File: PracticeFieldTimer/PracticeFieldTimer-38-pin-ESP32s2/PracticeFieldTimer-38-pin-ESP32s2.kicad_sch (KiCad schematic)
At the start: 17 parts, among them J1 RJ45, J2 4 x 20 I2C LCD, J3 DS3231 Module, J4 Panel, J5 RJ45, J6 Screw_Terminal_01x07, SW1 Reboot, SW2 Mode, SW3 Start/Cfg, U1 ESP32-DevKitC

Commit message: Clean up and assign most footprints. Need footprint for decoupling capacitor.
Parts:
- removed JP1: /CAN Enable, symbol Jumper:Jumper_2_Bridged
- added J1: /CAN Enable, Connector_PinHeader_2.54mm:PinHeader_1x02_P2.54mm_Vertical, symbol Connector:Conn_01x02_Pin
- D1, D2, D3: footprint (none) -> LED_THT:LED_D5.0mm
- J1, J5: footprint (none) -> Connector_RJ:RJ45_Amphenol_54602-x08_Horizontal
- J2: footprint (none) -> TerminalBlock:TerminalBlock_MaiXu_MX126-5.0-04P_1x04_P5.00mm
- J3: footprint (none) -> Connector_PinSocket_2.54mm:PinSocket_1x06_P2.54mm_Vertical
- J4: footprint (none) -> TerminalBlock:TerminalBlock_MaiXu_MX126-5.0-03P_1x03_P5.00mm
- J6: value Screw_Terminal_01x07 -> External Controls; footprint (none) -> TerminalBlock:TerminalBlock_MaiXu_MX126-5.0-07P_1x07_P5.00mm
- R3, R4: footprint (none) -> Resistor_THT:R_Axial_DIN0414_L11.9mm_D4.5mm_P5.08mm_Vertical
- SW1: footprint (none) -> Misc:SW_D6R40_F2_LFS
- SW2: footprint (none) -> Misc:2MS3T1B1M2QES
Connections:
- net GND: now also J1.2 (Pin_2)
- net at U1.10 (DAC_2/ADC2_CH9/GPIO26): now also J1.1 (Pin_1)

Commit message: Finish filling in footprints.
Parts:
- SW3: footprint (none) -> Misc:SW_D6R40_F2_LFS
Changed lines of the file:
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@@
 			)
 		)
-		(property "Footprint" ""
+		(property "Footprint" "Misc:SW_D6R40_F2_LFS"
 			(at 246.38 82.55 0)
 			(effects

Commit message: Resolved most errors. Still need to add mounting holes and define the board boundary. Also, the I2C header is way too close to the LCD and need to move. The required changes are unclear.
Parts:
- removed SW1: Reboot, Misc:SW_D6R40_F2_LFS, symbol Switch:SW_Push
- removed SW2: Mode, Misc:2MS3T1B1M2QES, symbol Switch:SW_SPDT
- removed SW3: Start/Cfg, Misc:SW_D6R40_F2_LFS, symbol Switch:SW_Push
- added S1: /RST, Misc:MJTP1119, symbol 2026-05-09_14-50-17:MJTP1119
- added S2: /CFG-START, Misc:MJTP1119, symbol 2026-05-09_14-50-17:MJTP1119
- added S3: 500ASSP1M2QE, Misc:SW_500ASSP1M2QE, symbol 2026-05-09_14-50-17:500ASSP1M2QE
- added U3: ~, Misc:LCD-I2C-20X4B-Breakout, symbol 2026-05-09_14-50-17:I2C_LCD_20x4
- J4: renamed from J3; footprint Connector_PinSocket_2.54mm:PinSocket_1x06_P2.54mm_Vertical -> Misc:DS3231_Module
- R3, R4: footprint Resistor_THT:R_Axial_DIN0414_L11.9mm_D4.5mm_P5.08mm_Vertical -> Resistor_THT:R_Axial_DIN0207_L6.3mm_D2.5mm_P15.24mm_Horizontal
- R5: footprint (none) -> Resistor_THT:R_Axial_DIN0207_L6.3mm_D2.5mm_P15.24mm_Horizontal
- renumbered J6 to J1, J4 to J3, J1 to J5, J5 to J6, J1 to J7
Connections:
- net GND: now also S1.1 (COM_1), S2.1 (COM_1), S3.2
- net /CFG-START: now also S2.2 (COM_2)
- net /Follow: now also S3.1
- net /Manual: now also S3.3
- net /RST: now also S1.2 (COM_2)
- no-connect marks 5 -> 28

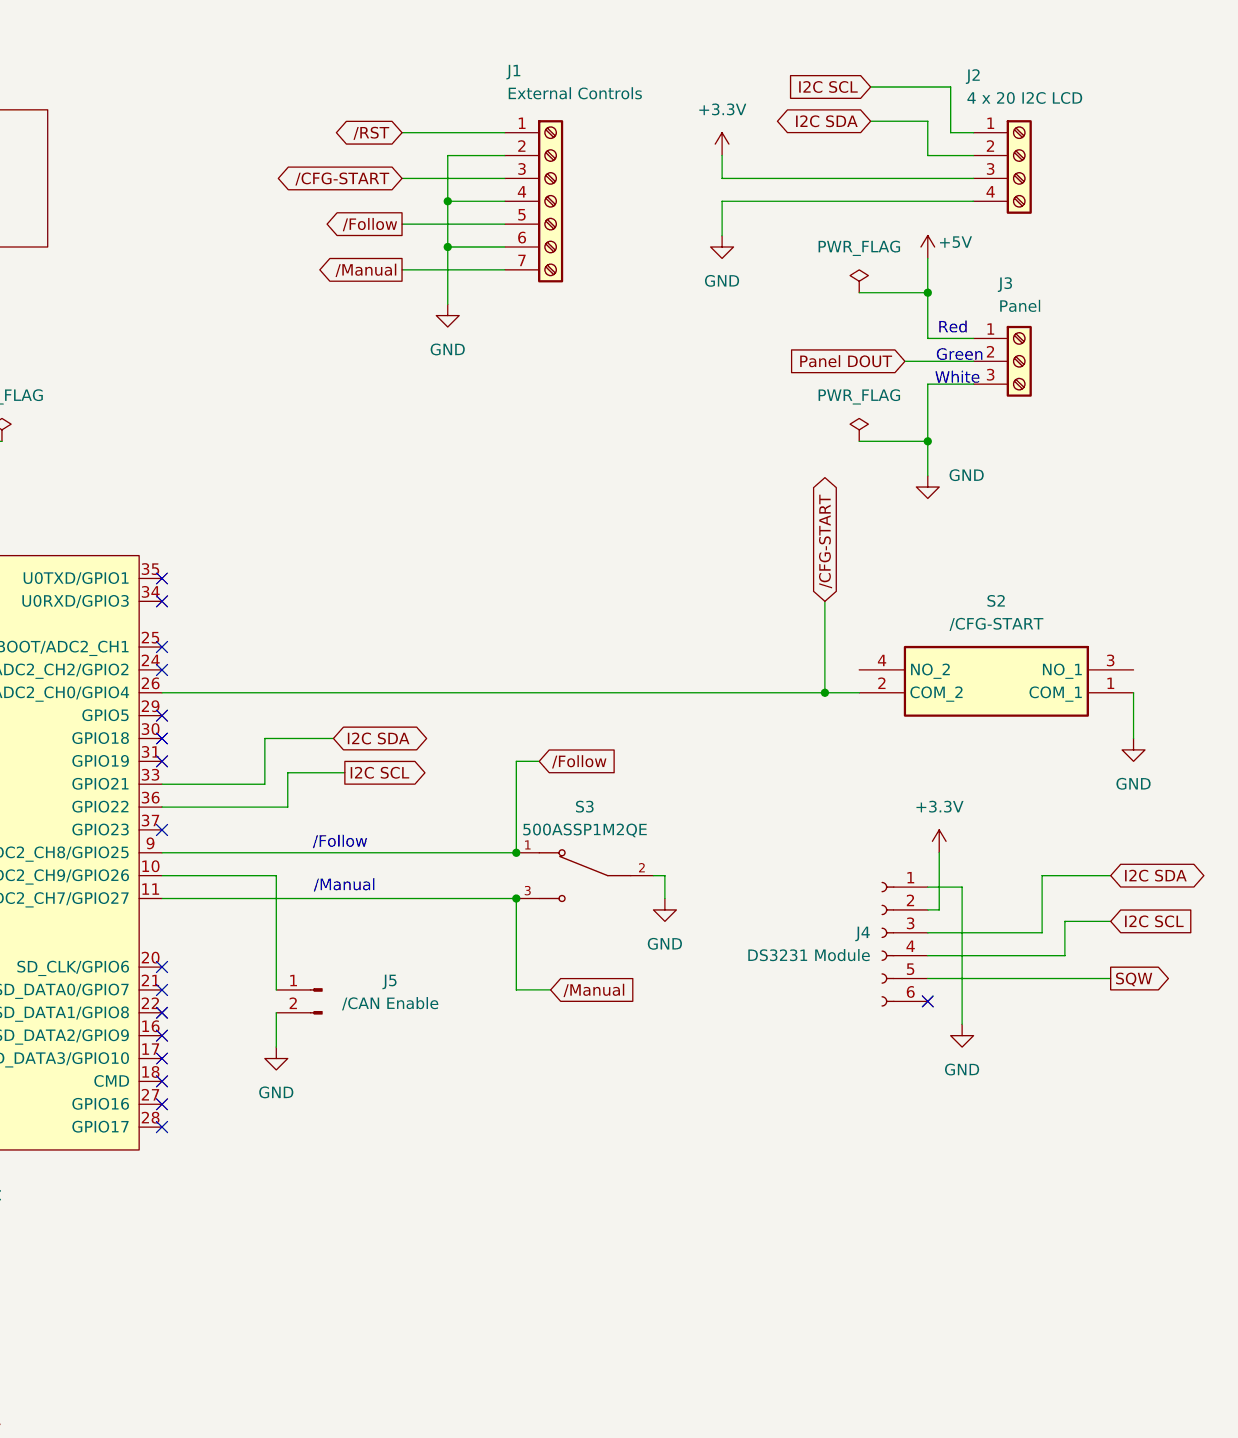
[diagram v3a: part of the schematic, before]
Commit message: Fix LCD header, which was wired backwards.
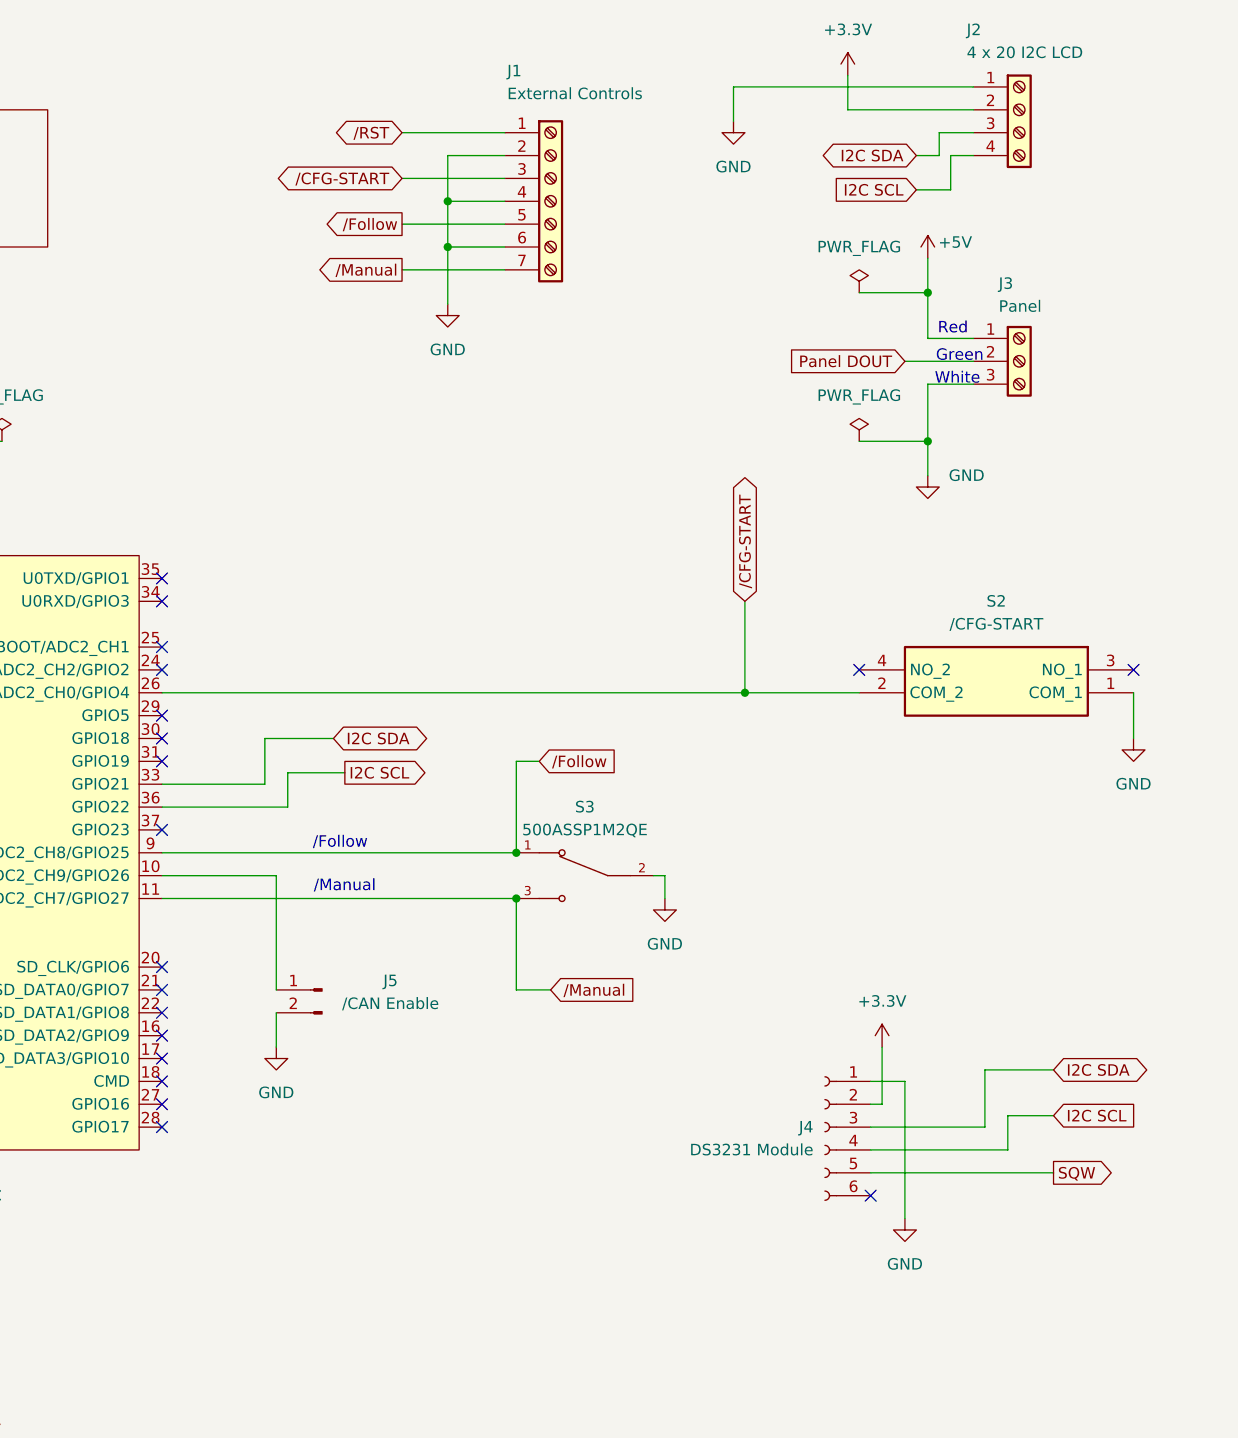
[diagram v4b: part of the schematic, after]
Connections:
- net +3.3V: now also J2.2 (Pin_2); no longer J2.3 (Pin_3)
- net GND: now also J2.1 (Pin_1); no longer J2.4 (Pin_4)
- net I2C SCL: now also J2.4 (Pin_4); no longer J2.1 (Pin_1)
- net I2C SDA: now also J2.3 (Pin_3); no longer J2.2 (Pin_2)
- no-connect marks 28 -> 30
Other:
- moved on the sheet: J2, J4

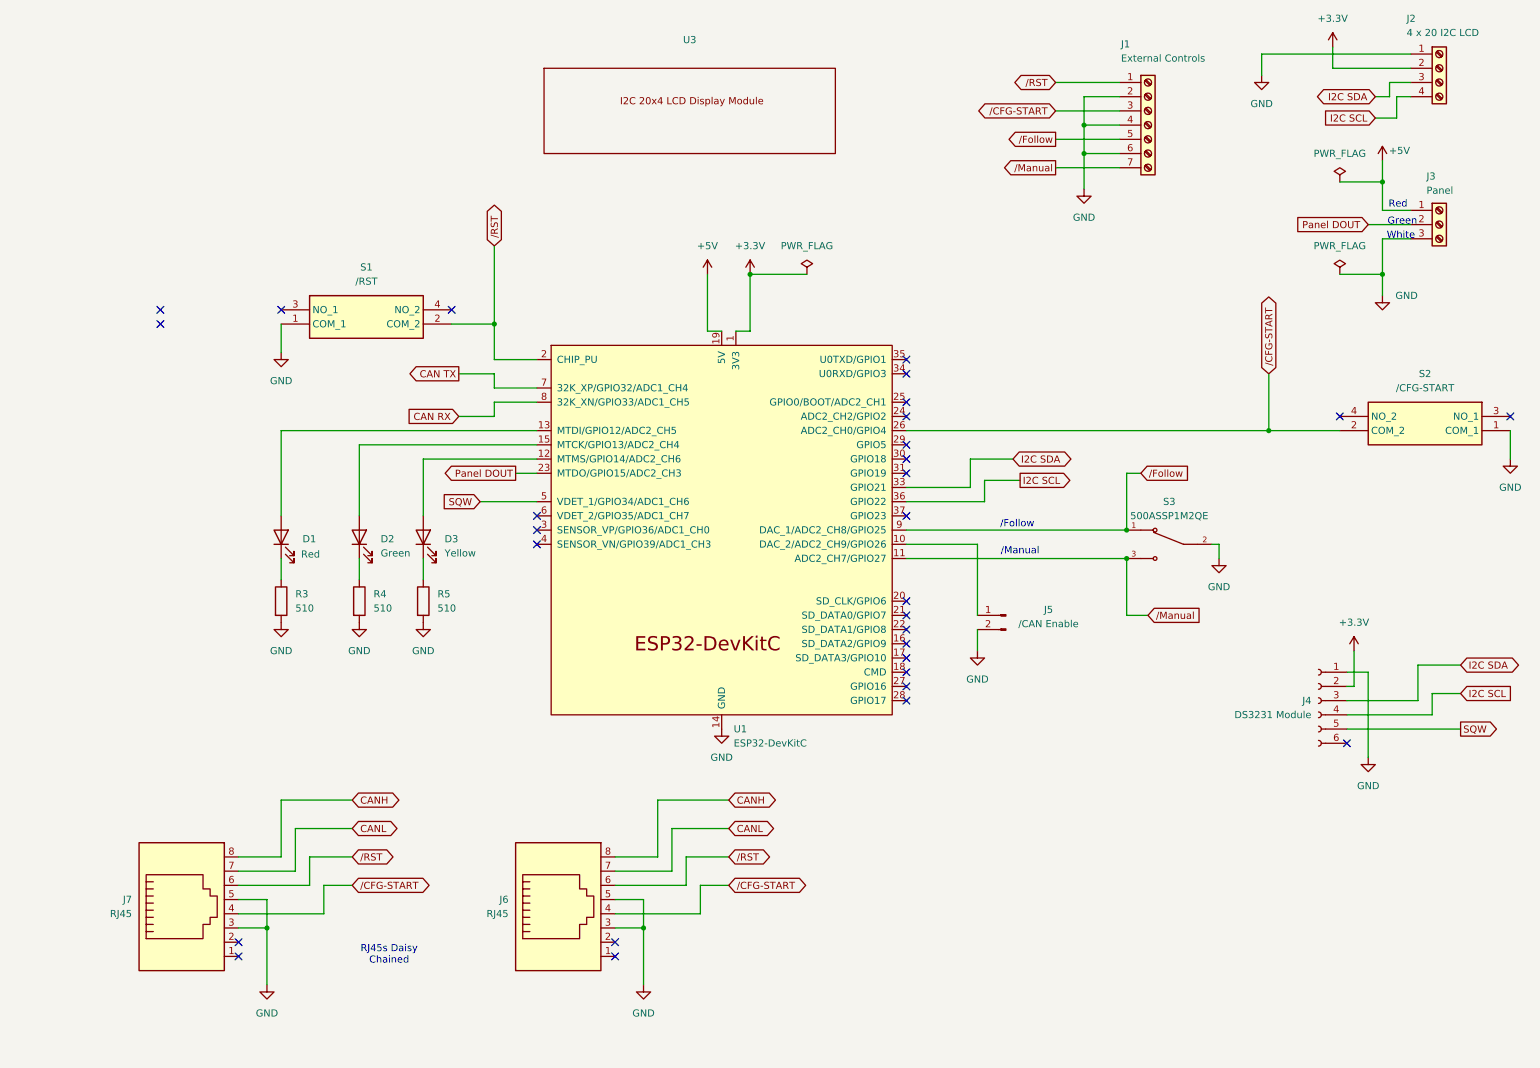
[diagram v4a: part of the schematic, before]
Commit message: Set schematic size to US Letter and adjust placements to fit. Add copyright notice and team logo.
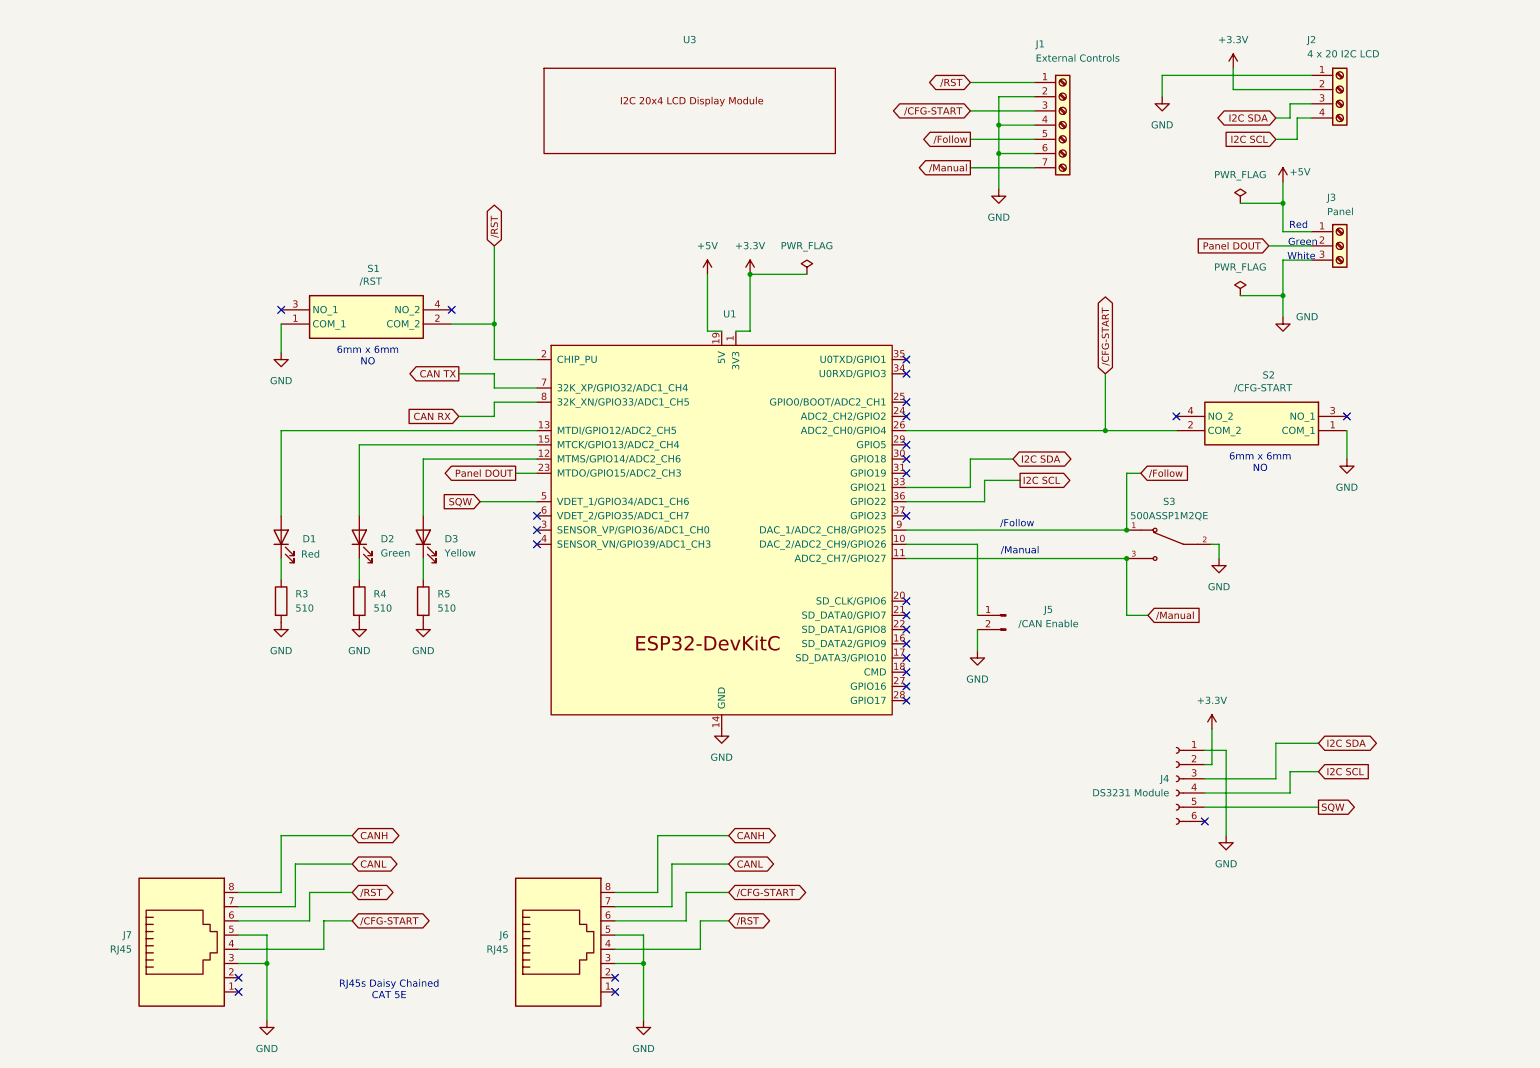
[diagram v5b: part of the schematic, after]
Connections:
- net /CFG-START: now also J6.6; no longer J6.4
- net /RST: now also J6.4; no longer J6.6
- no-connect marks 30 -> 28
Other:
- note added: "6mm x 6mm NO"
- note added: "RJ45s Daisy Chained CAT 5E"
- note removed: "RJ45s Daisy Chained"
- moved on the sheet: J1, J2, J3, J4, J6, J7, S2
